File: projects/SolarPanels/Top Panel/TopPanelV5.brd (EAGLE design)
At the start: 99 x 85.1 mm, 44 parts

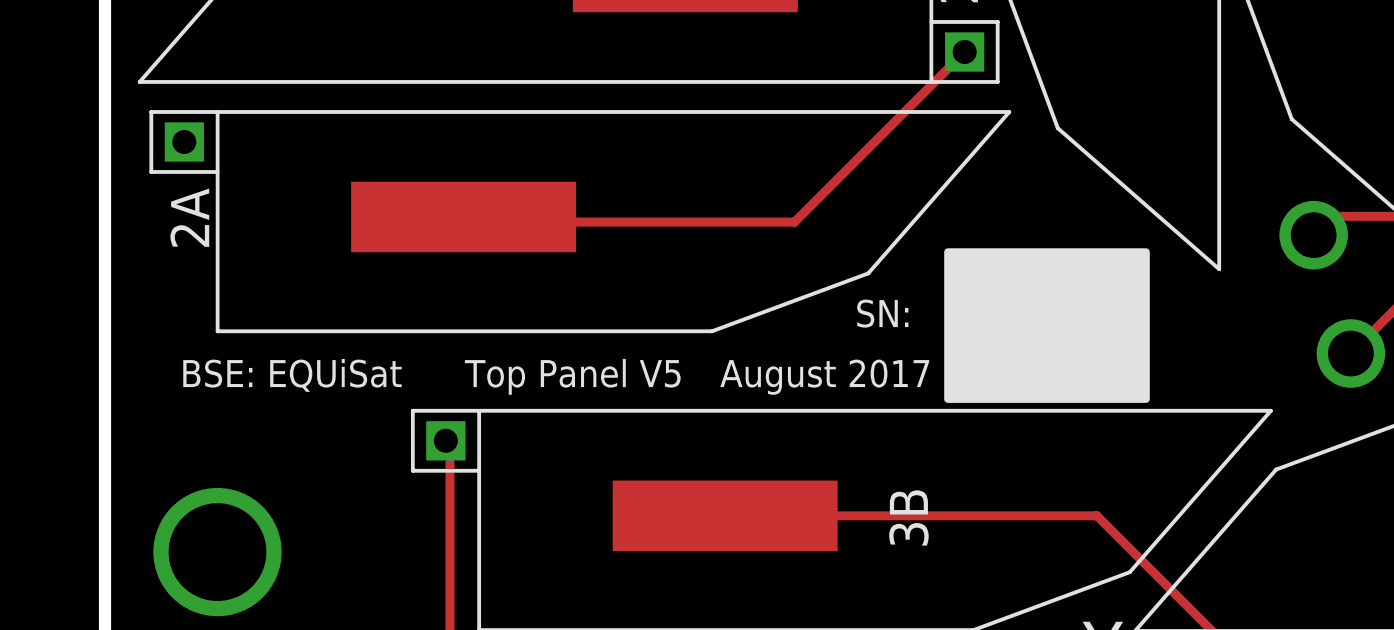
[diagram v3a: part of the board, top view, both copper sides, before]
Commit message: Added RBF switches to library. (changed ABF to RBF) Added RBF switches and routing to RBF Panel. Vectorized all text on solar panel boards and rearranged as needed.
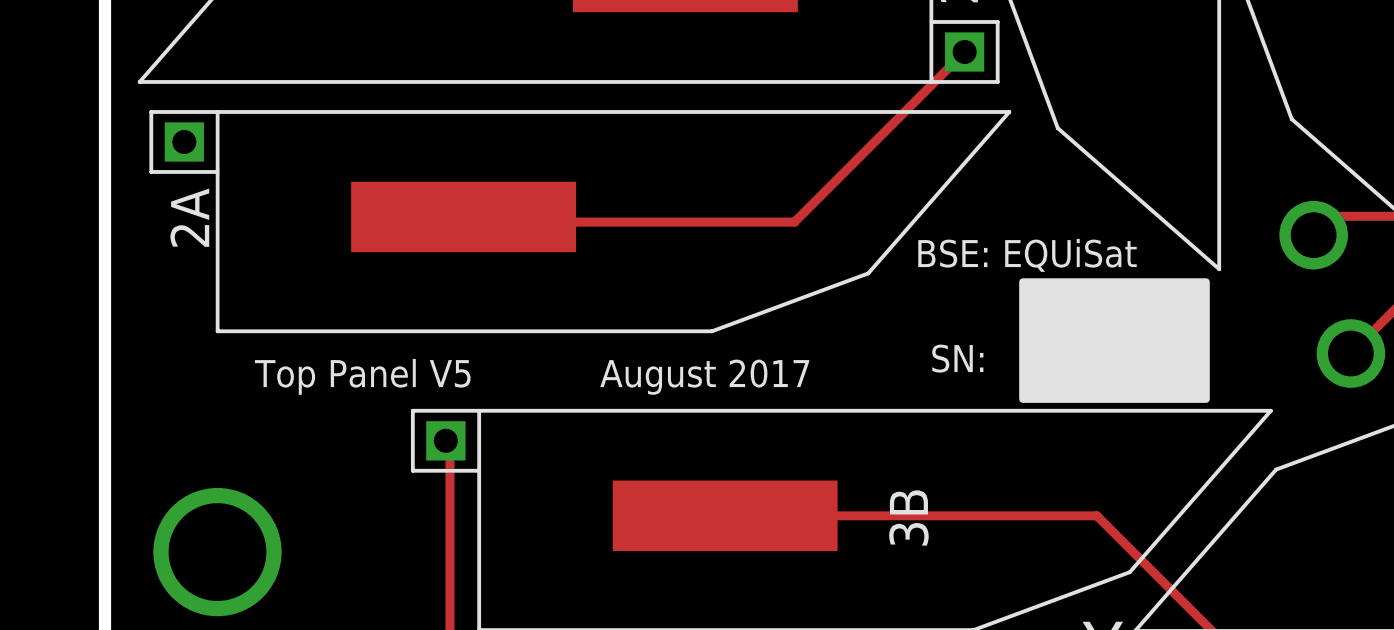
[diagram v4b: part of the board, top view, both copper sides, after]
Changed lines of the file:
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@@
 <drawing>
 <settings>
-<setting alwaysvectorfont="no"/>
+<setting alwaysvectorfont="yes"/>
 <setting verticaltext="up"/>
 </settings>
@@
 </polygon>
 <polygon width="0.254" layer="21">
-<vertex x="19.1" y="23.5"/>
-<vertex x="25.7" y="23.5"/>
-<vertex x="25.7" y="18.6"/>
-<vertex x="19.1" y="18.6"/>
+<vertex x="21.6" y="22.5"/>
+<vertex x="27.7" y="22.5"/>
+<vertex x="27.7" y="18.6"/>
+<vertex x="21.6" y="18.6"/>
 </polygon>
 <polygon width="0.254" layer="22">
@@
 <vertex x="-5.2" y="30.5"/>
 </polygon>
-<text x="-6.5" y="19" size="0.9" layer="25">BSE: EQUiSat</text>
-<text x="3" y="19" size="0.9" layer="25">Top Panel V5</text>
-<text x="16" y="21" size="0.9" layer="25">SN:</text>
-<text x="11.5" y="19" size="0.9" layer="25">August 2017</text>
+<text x="18" y="23" size="0.9" layer="25">BSE: EQUiSat</text>
+<text x="-4" y="19" size="0.9" layer="25">Top Panel V5</text>
+<text x="18.5" y="19.5" size="0.9" layer="25">SN:</text>
+<text x="7.5" y="19" size="0.9" layer="25">August 2017</text>
 <text x="46.8" y="73.4" size="1.778" layer="26" rot="MR0">+Y</text>
 <text x="22.8" y="9.4" size="1.778" layer="25">-Y</text>
 <text x="40.3" y="8.9" size="1.778" layer="26" rot="MR0">-Y</text>
-<text x="18.5" y="49" size="0.9" layer="26" rot="MR180">Brown Space Engineering: EQUiSat</text>
-<text x="31" y="47.5" size="0.9" layer="26" rot="MR180">Top Panel V5</text>
-<text x="38.5" y="45" size="0.9" layer="26" rot="MR0">August 2017</text>
+<text x="14.5" y="49" size="0.9" layer="26" rot="MR180">Brown Space Engineering: EQUiSat</text>
+<text x="29.5" y="47.5" size="0.9" layer="26" rot="MR180">Top Panel V5</text>
+<text x="40.5" y="45" size="0.9" layer="26" rot="MR0">August 2017</text>
 <text x="33.5" y="43" size="0.9" layer="26" rot="MR0">SN:</text>
 <text x="-7.7" y="49.9" size="1.778" layer="25">-X</text>
